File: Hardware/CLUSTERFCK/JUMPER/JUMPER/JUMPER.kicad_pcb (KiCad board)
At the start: 2 copper layers, 142 x 53.3 mm, 2 parts, among them J1 Conn_02x20_Counter_Clockwise, J2 Conn_02x20_Counter_Clockwise

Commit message: 0059 | 0,5h | Review JUMPER
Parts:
- moved J1 0.98 mm to (6.64, 50.8)
- moved J2 0.74 mm to (135.4, 2.53)
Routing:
- net +5V: track 312.4 -> 315.9 mm
- net /ADDR7: track 130.5 -> 132.4 mm
- net EXT2: track 130.5 -> 132.3 mm
- net zero: track 130.5 -> 132.2 mm
- net CLK: track 130.5 -> 132.2 mm
- net ~BI: track 130.5 -> 132.2 mm
- net /ADDR6: track 130.5 -> 132.2 mm
- net /ADDR2: track 130.5 -> 132.2 mm
- net /ADDR10: track 130.5 -> 132.2 mm
- net ~AI: track 130.5 -> 132.2 mm
- net carry: track 130.5 -> 132.2 mm
- net SU: track 130.5 -> 132.2 mm
- net EXT1: track 130.5 -> 132.2 mm
- net EXT0: track 130.5 -> 132.2 mm
- net /ADDR9: track 130.5 -> 132.2 mm
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
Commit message: 0065 | 24h | ADDR & DATA & PLACEHOLDER etc
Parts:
- moved J1 0.50 mm to (6.64, 50.3)
- moved J2 0.50 mm to (135.4, 2.03)
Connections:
- net carry renamed CARRY
- net zero renamed ZERO
- J1 pad 31: (no net) -> /DATA0
- J1 pad 32: (no net) -> /DATA1
- J1 pad 33: (no net) -> /DATA2
- J1 pad 34: (no net) -> /DATA3
- J1 pad 35: (no net) -> /DATA4
- J1 pad 36: (no net) -> /DATA5
- J1 pad 37: (no net) -> /DATA6
- J1 pad 38: (no net) -> /DATA7
- J2 pad 10: (no net) -> /DATA0
- J2 pad 3: (no net) -> /DATA7
- J2 pad 4: (no net) -> /DATA6
- J2 pad 5: (no net) -> /DATA5
- J2 pad 6: (no net) -> /DATA4
- J2 pad 7: (no net) -> /DATA3
- J2 pad 8: (no net) -> /DATA2
- J2 pad 9: (no net) -> /DATA1
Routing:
- net /DATA3: track 0.00 -> 132.4 mm
- net /DATA1: track 0.00 -> 132.4 mm
- net /DATA7: track 0.00 -> 132.2 mm
- net /DATA6: track 0.00 -> 132.2 mm
- net /DATA5: track 0.00 -> 132.2 mm
- net /DATA4: track 0.00 -> 132.2 mm
- net /DATA2: track 0.00 -> 132.2 mm
- net /DATA0: track 0.00 -> 132.2 mm
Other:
- board size 142 x 53.3 mm -> 142 x 52.3 mm

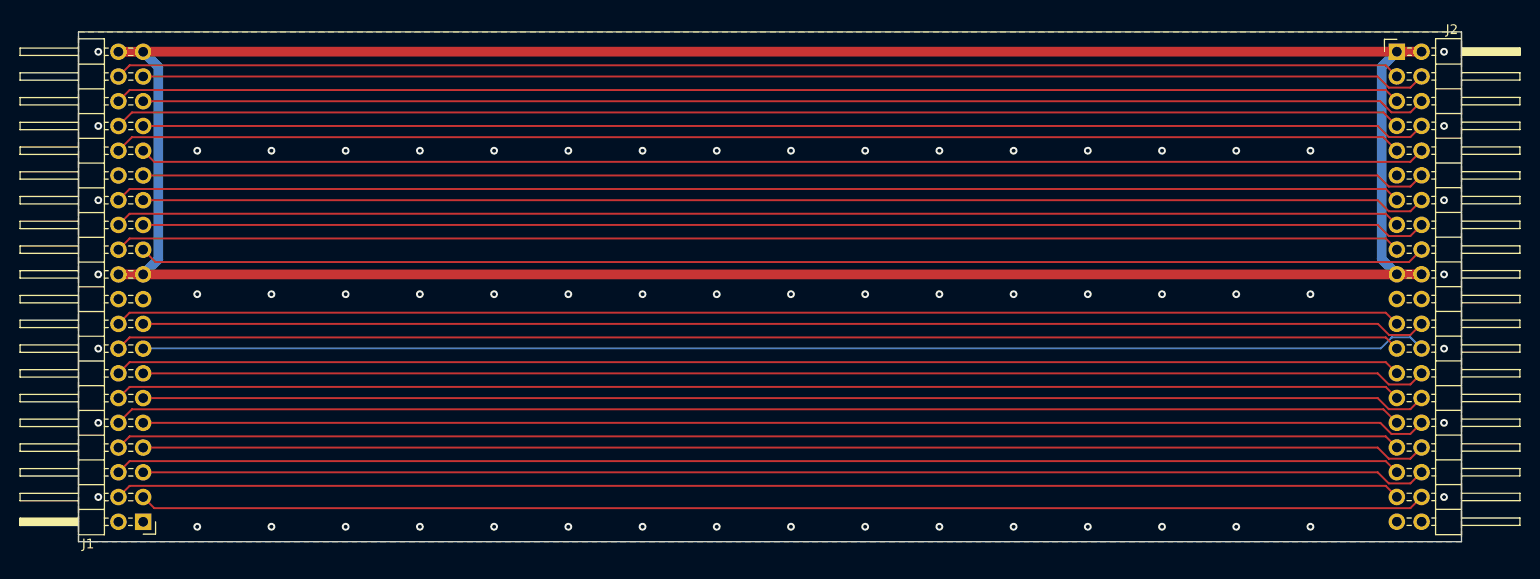
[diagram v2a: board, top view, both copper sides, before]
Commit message: added JLC logo to JMPER
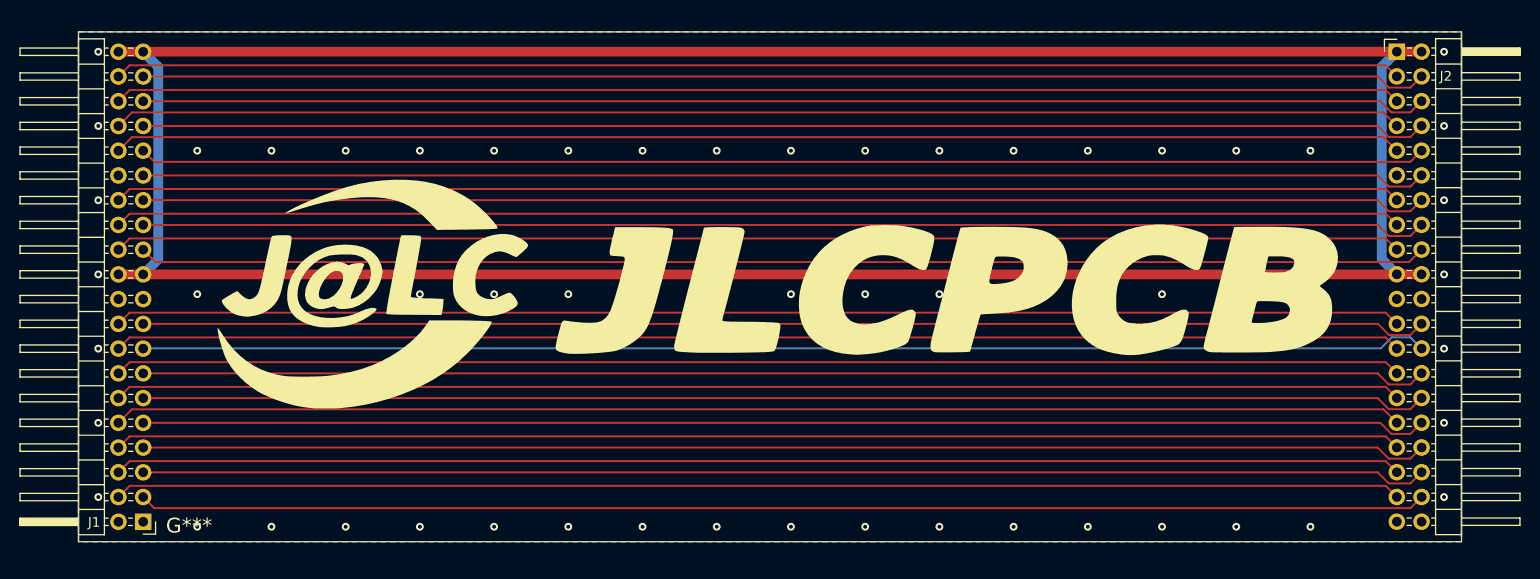
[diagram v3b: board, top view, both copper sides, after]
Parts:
- added G***: LOGO, LOGO, F.Cu at (71.8, 26.9)

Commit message: 0072 | 3h | make silkscreen prettier
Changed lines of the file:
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@@
     (at 71.8 26.9)
     (attr through_hole)
-    (fp_text reference "G***" (at -60.45 23.8) (layer "F.SilkS")
+    (fp_text reference "G***" (at -60.34 23.51) (layer "F.SilkS")
       (effects (font (size 1.524 1.524) (thickness 0.3)))
     )
@@
   (via (at 111.252 26.932) (size 0.8) (drill 0.4) (layers "F.Cu" "B.Cu") (free) (net 9))
   (via (at 65.532 12.2) (size 0.8) (drill 0.4) (layers "F.Cu" "B.Cu") (free) (net 9))
-  (via (at 35.052 26.932) (size 0.8) (drill 0.4) (layers "F.Cu" "B.Cu") (free) (net 9))
+  (via (at 35.01 26.81) (size 0.8) (drill 0.4) (layers "F.Cu" "B.Cu") (free) (net 9))
   (via (at 65.532 26.932) (size 0.8) (drill 0.4) (layers "F.Cu" "B.Cu") (free) (net 9))
   (via (at 126.492 50.808) (size 0.8) (drill 0.4) (layers "F.Cu" "B.Cu") (free) (net 9))
@@
   (via (at 27.432 12.2) (size 0.8) (drill 0.4) (layers "F.Cu" "B.Cu") (free) (net 9))
   (via (at 57.912 50.808) (size 0.8) (drill 0.4) (layers "F.Cu" "B.Cu") (free) (net 9))
-  (via (at 88.392 26.932) (size 0.8) (drill 0.4) (layers "F.Cu" "B.Cu") (free) (net 9))
+  (via (at 88.31 26.932) (size 0.8) (drill 0.4) (layers "F.Cu" "B.Cu") (free) (net 9))
   (via (at 19.812 12.2) (size 0.8) (drill 0.4) (layers "F.Cu" "B.Cu") (free) (net 9))
   (via (at 2.032 2.04) (size 0.8) (drill 0.4) (layers "F.Cu" "B.Cu") (free) (net 9))
